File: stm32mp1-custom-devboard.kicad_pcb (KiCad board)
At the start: 4 copper layers, 120 x 72 mm, 40 parts, among them Con1 52746-0671, Con2 505110-2491, U1 TPS61169DCKR, U2 MCP1703T-3302E, U3 ST1S10PHR, U4 ST1S09IPUR

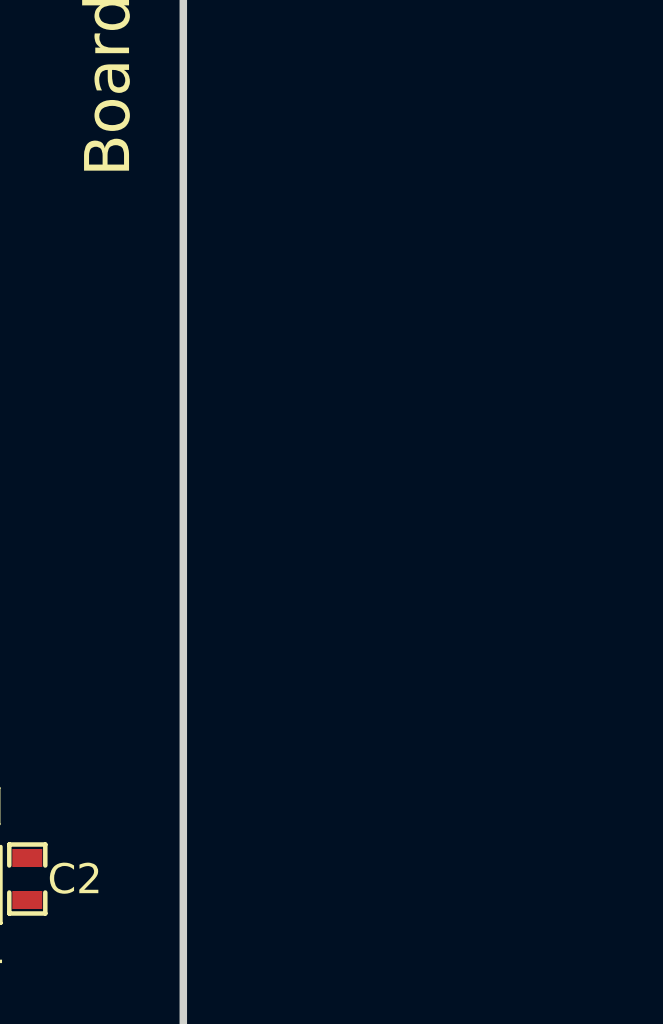
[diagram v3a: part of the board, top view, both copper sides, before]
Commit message: Added Mipi Dsi connection, started stlink module
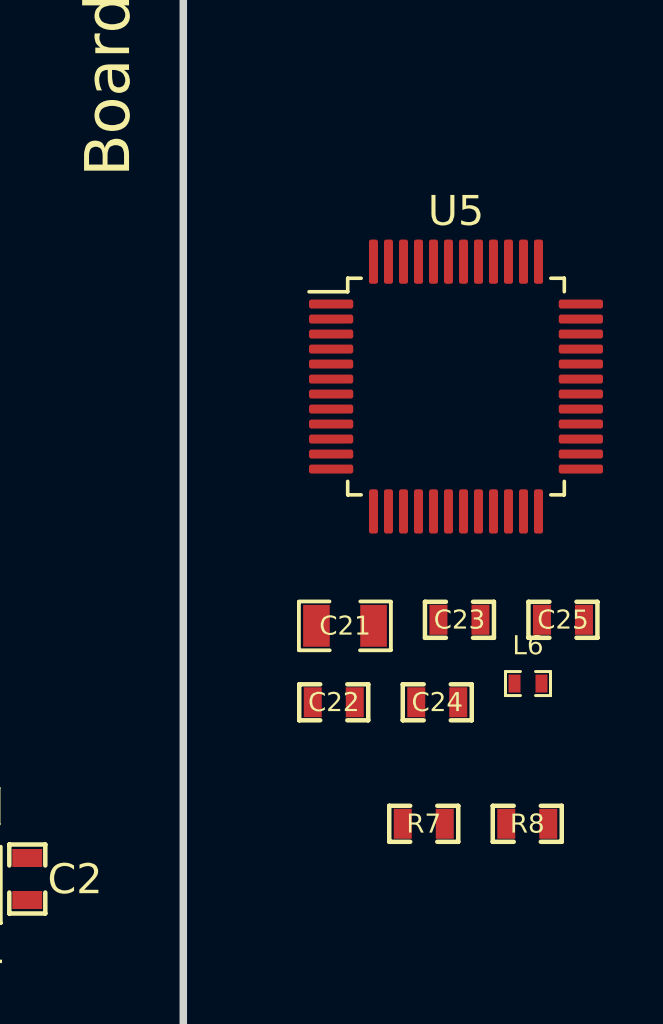
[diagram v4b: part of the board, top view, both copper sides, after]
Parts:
- added C21: 10uF/6V3, Capacitors_Smd_0805:10uF_0805, F.Cu at (218.5, 123.7)
- added C22: 100nF/50V, Capacitors_Smd_0603:100nF_0603, F.Cu at (218.1, 126.2)
- added C23: 100nF/50V, Capacitors_Smd_0603:100nF_0603, F.Cu at (222.3, 123.5)
- added C24: 100nF/50V, Capacitors_Smd_0603:100nF_0603, F.Cu at (221.6, 126.2)
- added C25: 100nF/50V, Capacitors_Smd_0603:100nF_0603, F.Cu at (225.8, 123.5)
- added L6: BLM15HG601SN1D, Inductors:BLM15HG601SN1D_0402, F.Cu at (224.6, 125.6)
- added R7: 4k7, Resistor_Smd_0603:4k7_0603, F.Cu at (221.1, 130.3)
- added R8: 4k7, Resistor_Smd_0603:4k7_0603, F.Cu at (224.6, 130.3)
- added U5: STM32F103C(8-B)Tx, Stm32_Microcontrollers:STM32F103CBT6, F.Cu at (222.2, 115.7)
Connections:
- net /LCD+Touchscreen/LCD_LED+ renamed /LCD+Touchscreen/LCD Backlight Controller/BACKLIGHT_HIGH
- net /LCD+Touchscreen/LCD_LED- renamed /LCD+Touchscreen/LCD Backlight Controller/BACKLIGHT_LOW
- net /Power Supply Module/POWER_OUT_5V_3A renamed 5V
- C1 pad 1: VDD -> 3V3
- C16 pad 1: /Power Supply Module/POWER_OUT_3V3_2A -> 3V3
- C3 pad 1: VDD -> 3V3
- Con1 pad 3: (no net) -> /STM32MP1 module/PA14_IRQ
- Con1 pad 4: (no net) -> /STM32MP1 module/PE2_I2C4_SDA
- Con1 pad 5: (no net) -> /STM32MP1 module/PE2_I2C4_SCL
- Con1 pad 6: (no net) -> /STM32MP1 module/PF10_GPIO
- Con2 pad 12: (no net) -> /LCD+Touchscreen/LCD_RESET
- Con2 pad 13: (no net) -> /LCD+Touchscreen/LCD_TE
- Con2 pad 15: (no net) -> /LCD+Touchscreen/LCD_MIPI_CLK+
- Con2 pad 16: (no net) -> /LCD+Touchscreen/LCD_MIPI_CLK-
- Con2 pad 18: (no net) -> /LCD+Touchscreen/LCD_MIPI_D1+
- Con2 pad 19: (no net) -> /LCD+Touchscreen/LCD_MIPI_D1-
- Con2 pad 21: (no net) -> /LCD+Touchscreen/LCD_MIPI_D0+
- Con2 pad 22: (no net) -> /LCD+Touchscreen/LCD_MIPI_D0-
- L2 pad 2: /Power Supply Module/POWER_OUT_3V3_2A -> 3V3
- L3 pad 1: VDD -> 3V3
- R3 pad 1: /Power Supply Module/POWER_OUT_3V3_2A -> 3V3
- SOM1 pad 1: (no net) -> GND
- SOM1 pad 100: (no net) -> Net-(SOM1-Pad100)
- SOM1 pad 102: (no net) -> Net-(SOM1-Pad100)
- SOM1 pad 103: (no net) -> GND
- SOM1 pad 104: (no net) -> Net-(SOM1-Pad100)
- SOM1 pad 106: (no net) -> Net-(SOM1-Pad100)
- SOM1 pad 107: (no net) -> GND
- SOM1 pad 108: (no net) -> Net-(SOM1-Pad100)
- SOM1 pad 110: (no net) -> Net-(SOM1-Pad100)
- SOM1 pad 111: (no net) -> /LCD+Touchscreen/LCD_BACKLIGHT_PWM
- SOM1 pad 112: (no net) -> Net-(SOM1-Pad100)
- SOM1 pad 115: (no net) -> GND
- SOM1 pad 116: (no net) -> GND
- SOM1 pad 117: (no net) -> /STM32MP1 module/PA14_IRQ
- SOM1 pad 120: (no net) -> GND
- SOM1 pad 121: (no net) -> /STM32MP1 module/PE2_I2C4_SCL
- SOM1 pad 125: (no net) -> GND
- SOM1 pad 127: (no net) -> GND
- SOM1 pad 128: (no net) -> GND
- SOM1 pad 130: (no net) -> GND
- SOM1 pad 132: (no net) -> GND
- SOM1 pad 135: (no net) -> GND
- SOM1 pad 136: (no net) -> GND
- SOM1 pad 146: (no net) -> GND
- SOM1 pad 147: (no net) -> GND
- SOM1 pad 15: (no net) -> GND
- SOM1 pad 156: (no net) -> GND
- SOM1 pad 157: (no net) -> /LCD+Touchscreen/LCD_RESET
- SOM1 pad 159: (no net) -> GND
- SOM1 pad 165: (no net) -> GND
- SOM1 pad 168: (no net) -> GND
- SOM1 pad 17: (no net) -> GND
- SOM1 pad 170: (no net) -> GND
- SOM1 pad 172: (no net) -> GND
- SOM1 pad 174: (no net) -> GND
- SOM1 pad 176: (no net) -> GND
- SOM1 pad 177: (no net) -> GND
- SOM1 pad 178: (no net) -> GND
- SOM1 pad 180: (no net) -> GND
- SOM1 pad 181: (no net) -> GND
- SOM1 pad 182: (no net) -> GND
- SOM1 pad 184: (no net) -> GND
- SOM1 pad 185: (no net) -> GND
- SOM1 pad 186: (no net) -> /LCD+Touchscreen/LCD_MIPI_D0-
- SOM1 pad 188: (no net) -> /LCD+Touchscreen/LCD_MIPI_D0+
- SOM1 pad 189: (no net) -> GND
- SOM1 pad 192: (no net) -> /LCD+Touchscreen/LCD_MIPI_D1-
- SOM1 pad 193: (no net) -> /LCD+Touchscreen/LCD_MIPI_CLK-
- SOM1 pad 194: (no net) -> /LCD+Touchscreen/LCD_MIPI_D1+
- SOM1 pad 195: (no net) -> /LCD+Touchscreen/LCD_MIPI_CLK+
- SOM1 pad 199: (no net) -> GND
- SOM1 pad 2: (no net) -> GND
- SOM1 pad 20: (no net) -> GND
- SOM1 pad 200: (no net) -> GND
- SOM1 pad 22: (no net) -> GND
- SOM1 pad 23: (no net) -> GND
- SOM1 pad 26: (no net) -> GND
- SOM1 pad 28: (no net) -> GND
- SOM1 pad 29: (no net) -> GND
- SOM1 pad 35: (no net) -> GND
- SOM1 pad 38: (no net) -> GND
- SOM1 pad 40: (no net) -> GND
- SOM1 pad 41: (no net) -> GND
- SOM1 pad 49: (no net) -> /LCD+Touchscreen/LCD_TE
- SOM1 pad 50: (no net) -> GND
- SOM1 pad 51: (no net) -> GND
- SOM1 pad 56: (no net) -> /STM32MP1 module/PE2_I2C4_SDA
- SOM1 pad 59: (no net) -> GND
- SOM1 pad 60: (no net) -> GND
- SOM1 pad 64: (no net) -> /STM32MP1 module/PF10_GPIO
- SOM1 pad 70: (no net) -> GND
- SOM1 pad 71: (no net) -> GND
- SOM1 pad 81: (no net) -> GND
- SOM1 pad 82: (no net) -> GND
- SOM1 pad 84: (no net) -> GND
- SOM1 pad 85: (no net) -> Net-(SOM1-Pad85)
- SOM1 pad 87: (no net) -> Net-(SOM1-Pad85)
- SOM1 pad 88: (no net) -> Net-(SOM1-Pad85)
- SOM1 pad 89: (no net) -> Net-(SOM1-Pad85)
- SOM1 pad 90: (no net) -> Net-(SOM1-Pad85)
- SOM1 pad 91: (no net) -> Net-(SOM1-Pad85)
- SOM1 pad 92: (no net) -> Net-(SOM1-Pad85)
- SOM1 pad 93: (no net) -> Net-(SOM1-Pad85)
- SOM1 pad 96: (no net) -> Net-(SOM1-Pad100)
- SOM1 pad 98: (no net) -> Net-(SOM1-Pad100)
- U1 pad 4: (no net) -> /LCD+Touchscreen/LCD_BACKLIGHT_PWM
- U1 pad 5: VDD -> 3V3
- U2 pad 3: VDD -> 3V3

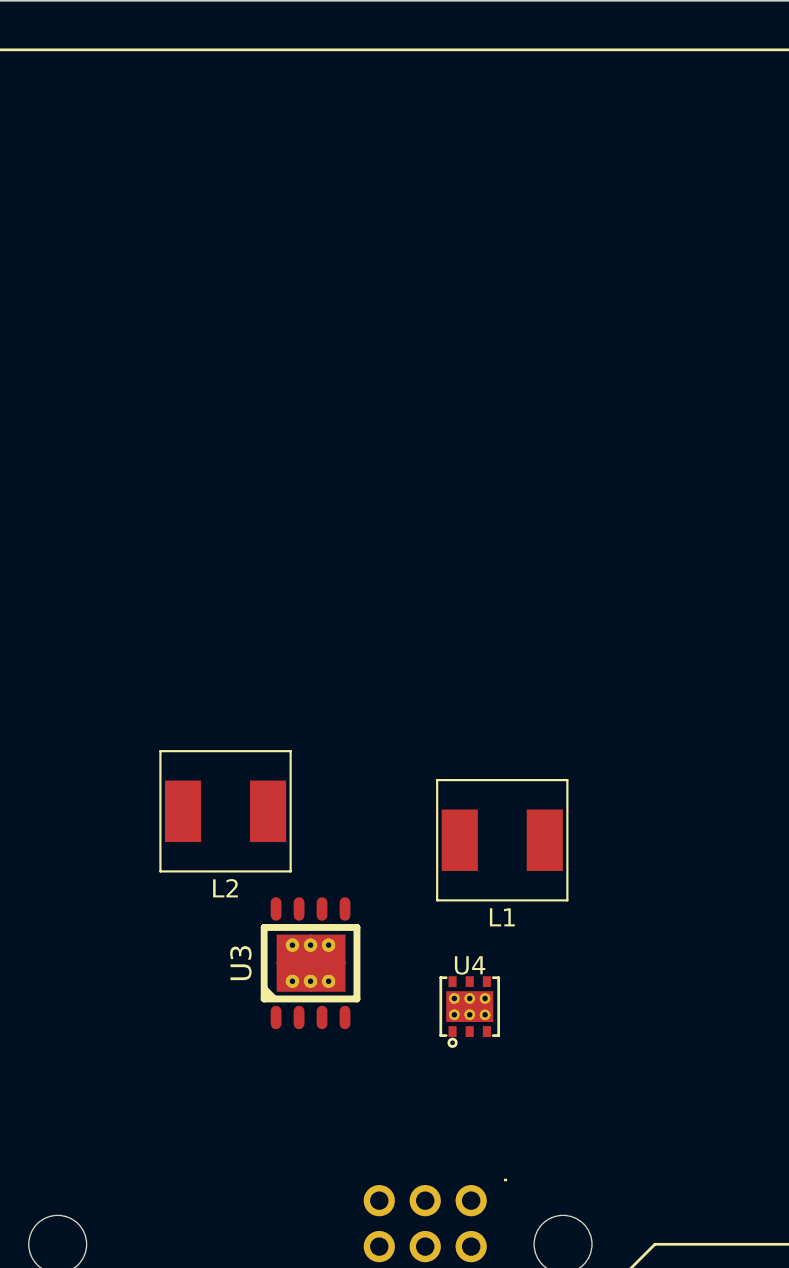
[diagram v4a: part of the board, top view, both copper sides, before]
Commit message: Added minipci connector
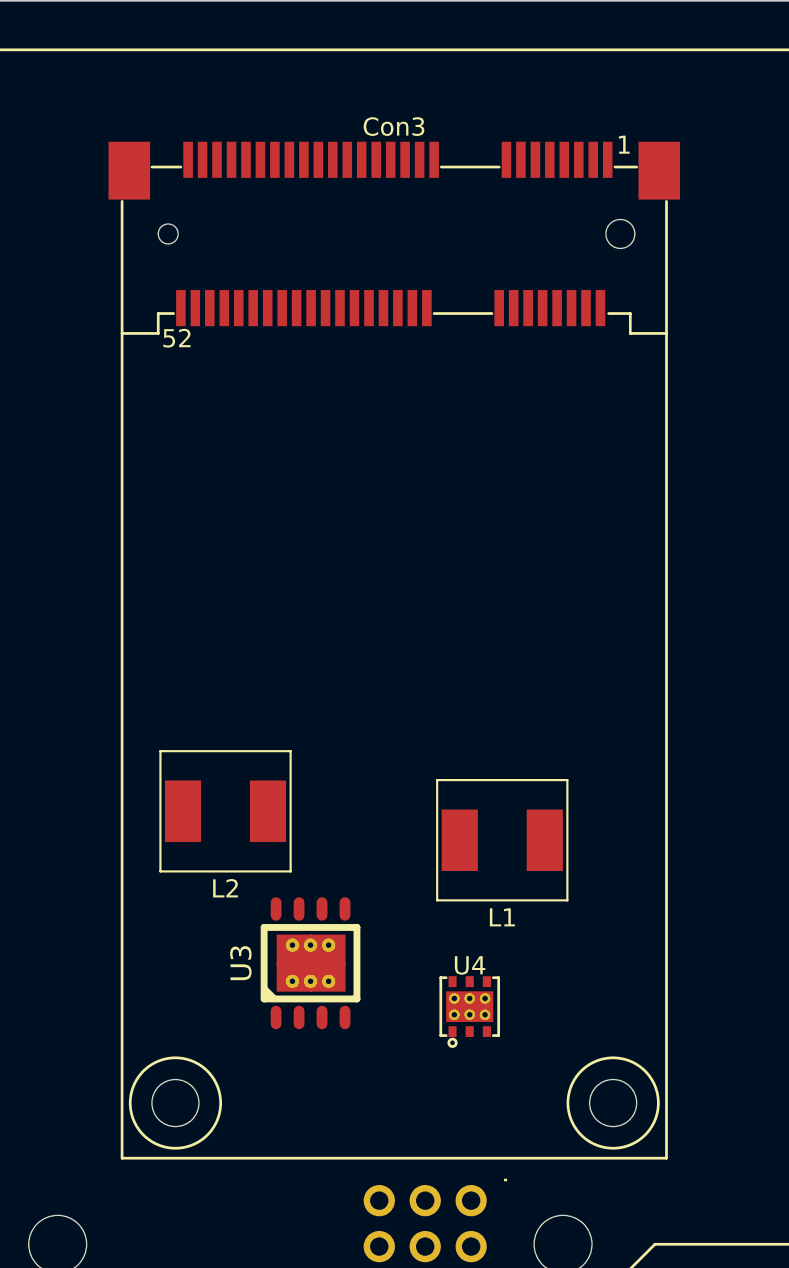
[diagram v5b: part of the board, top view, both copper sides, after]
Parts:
- added Con3: 2041119-1, Smd_Connectors:2041119-1, F.Cu at (157.4, 79.4)

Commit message: Finished work at st-link, figurated elements on pcb
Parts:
- added C26: 1nF/2kV, Capacitors_Smd_1206:1nF_2kV_1206, F.Cu at (210.1, 81.8)
- added C27: 100n/50V, Capacitors_Smd_0603:100nF_0603, F.Cu at (187.3, 74.2)
- added C28: 100nF/50V, Capacitors_Smd_0603:100nF_0603, F.Cu at (192.5, 68.4)
- added C29: 100nF/50V, Capacitors_Smd_0603:100nF_0603, F.Cu at (192.9, 73.4)
- added C30: 10uF/6V3, Capacitors_Smd_0805:10uF_0805, F.Cu at (196.0, 72.3)
- added C31: 20pF/50V, Capacitors_Smd_0603:20pF_0603, F.Cu at (182.8, 78.4)
- added C32: 20pF/50V, Capacitors_Smd_0603:20pF_0603, F.Cu at (186.4, 84.9)
- added Con4: USB_C_Wurth_632723130112, Connector_USB:USB_C_632723130112, F.Cu at (207.8, 73.5)
- added D2: BAT54C, Diodes:BAT54C, F.Cu at (193.2, 71.2)
- added D3: HSMF-C155, Diodes:HSMF-C155, F.Cu at (205.7, 81.0)
- added P1: Main Power Supply, Smd_Connectors:2060-452_998-404, F.Cu at (140.5, 74.3)
- added Q1: BC847B, Transistor_Bipolar:BC847B_SOT23, F.Cu at (200.2, 69.3)
- added R10: 10k, Resistor_Smd_0603:10k_0603, F.Cu at (201.7, 71.9)
- added R11: 36k, Resistor_Smd_0603:36k_0603, F.Cu at (196.2, 68.5)
- added R12: 22R, Resistor_Smd_0603:22R_0603, F.Cu at (200.3, 74.3)
- added R13: 1k5, Resistor_Smd_0603:1k5_0603, F.Cu at (198.8, 72.6)
- added R14: 100R, Resistor_Smd_0603:100R_0603, F.Cu at (197.6, 68.5)
- added R15: 22R, Resistor_Smd_0603:22R_0603, F.Cu at (201.7, 75.1)
- added R16: 220R, Resistor_Smd_0603:220R_0603, F.Cu at (202.8, 79.7)
- added R17: 220R, Resistor_Smd_0603:220R_0603, F.Cu at (202.8, 81.1)
- added R18: 10k, Resistor_Smd_0603:10k_0603, F.Cu at (189.3, 85.7)
- added R19: 4k7, Resistor_Smd_0603:4k7_0603, F.Cu at (187.3, 86.9)
- added R20: 10k, Resistor_Smd_0603:10k_0603, F.Cu at (189.3, 87.1)
- added R21: 100k, Resistor_Smd_0603:100k_0603, F.Cu at (192.9, 74.9)
- added R22: 4k7, Resistor_Smd_0603:4k7_0603, F.Cu at (192.0, 87.1)
- added R23: 100R, Resistor_Smd_0603:100R_0603, F.Cu at (201.4, 83.2)
- added R24: 0R, Resistor_Smd_0603:0R_0603, F.Cu at (197.0, 74.6)
- added R9: 100k, Resistor_Smd_0603:100k_0603, F.Cu at (188.7, 74.2)
- added U6: MCP1700T-3302E_MB, Linear:MCP1700T-3302E_MB_SOT89, F.Cu at (188.3, 70.3)
- added X1: 8.000MHZ, Resonators:ABM3AIG-8.000MHZ-8-1R-T, F.Cu at (186.5, 80.5)
- moved C7 68.1 mm to (140.9, 82.8), turned to 180 degrees
- moved C17 64.3 mm to (137.0, 93.3), turned to 90 degrees
- moved R5 61.3 mm to (136.1, 103.9), turned to 90 degrees
- moved C10 61.0 mm to (136.7, 98.6), turned to 180 degrees
- moved C9 60.9 mm to (139.2, 98.6), turned to 180 degrees
- moved C24 60.4 mm to (190.8, 74.2), turned to 90 degrees
- moved L5 60.2 mm to (146.5, 92.6), turned to 270 degrees
- moved C20 60.2 mm to (136.9, 101.8)
- moved C19 60.2 mm to (136.9, 100.4)
- moved R2 60.1 mm to (142.6, 99.2), turned to 180 degrees
- moved R6 59.2 mm to (136.1, 106.5), turned to 270 degrees
- moved C8 59.0 mm to (141.7, 86.3), turned to 180 degrees
- moved C23 57.4 mm to (189.5, 76.3), turned to 180 degrees
- moved L6 56.5 mm to (188.8, 81.9), turned to 90 degrees
- moved C15 54.2 mm to (137.5, 103.9), turned to 90 degrees
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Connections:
- C21 pad 1: Net-(C21-Pad1) -> 3V3
- C22 pad 1: Net-(C21-Pad1) -> 3V3
- C23 pad 1: Net-(C21-Pad1) -> 3V3
- C24 pad 1: Net-(C21-Pad1) -> 3V3
- C25 pad 1: Net-(C21-Pad1) -> 3V3
- L6 pad 2: Net-(C21-Pad1) -> 3V3
- U5 pad 1: Net-(C21-Pad1) -> 3V3
- U5 pad 10: (no net) -> Net-(R19-Pad2)
- U5 pad 2: (no net) -> Net-(R20-Pad1)
- U5 pad 20: (no net) -> GND
- U5 pad 24: Net-(C21-Pad1) -> 3V3
- U5 pad 25: (no net) -> Net-(R23-Pad2)
- U5 pad 27: (no net) -> /STLink Module/JTMS
- U5 pad 3: (no net) -> Net-(R18-Pad1)
- U5 pad 30: (no net) -> Net-(R16-Pad2)
- U5 pad 32: (no net) -> Net-(R12-Pad1)
- U5 pad 33: (no net) -> Net-(R15-Pad1)
- U5 pad 36: Net-(C21-Pad1) -> 3V3
- U5 pad 38: (no net) -> Net-(R14-Pad2)
- U5 pad 39: (no net) -> Net-(R24-Pad2)
- U5 pad 44: (no net) -> Net-(R21-Pad2)
- U5 pad 48: Net-(C21-Pad1) -> 3V3
- U5 pad 5: (no net) -> Net-(C31-Pad2)
- U5 pad 6: (no net) -> Net-(C32-Pad2)
- U5 pad 7: (no net) -> Net-(C27-Pad1)
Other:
- board text added: "STM32MP1 Development Board based on stm32mp1-Visionsom"
- board text removed: "STM32MP1 Development Board based on stm32mp1-visionsom"
